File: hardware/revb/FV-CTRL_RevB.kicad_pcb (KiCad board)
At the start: 2 copper layers, 100 x 100 mm, 152 parts, among them J1 12V INPUT, J10 IR RX2 3V3/OUT/G, J11 IR TX1 A/K, J12 IR TX2 A/K, J13 LS1 DNP, J14 LS2 DNP, J15 LS3 DNP, J16 LS4 DNP, J17 I2C 3V3/SDA/SCL/G, J2 XL4015 A: 12/G/6/G, J20 SMA 50ohm ANT, J21 USB MICRO DATA, J3 XL4015 B: 12/G/6/G, J4 5V D24V25F5, J5 S1_TOP, J6 S1_BOT, J7 S2_TOP, J8 S2_BOT, J9 IR RX1 3V3/OUT/G, Q1 IRF4905PBF, Q2 P2N2222AG, Q3 MMBT3904, Q4 MMBT3904, SW1 RESET, SW2 BOOT, U1 ESP32-D0WD-V3, U2 CP2102N-A02-GQFN24, U3 LD1117V33, U4 W25Q32JVSSIQ, U5 TLV803EA30DBZR, Y1 40MHz CL10pF

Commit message: fix(hardware): replace Pololu logic supply with RECOM 5V converter
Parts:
- added C57: 10uF 50V, Capacitor_THT:CP_Radial_D5.0mm_P2.00mm, F.Cu at (120.0, 124.5)
- added C58: 100nF, Capacitor_SMD:C_0402_1005Metric, F.Cu at (118.1, 141.2)
- J4: value 5V D24V25F5 -> 5V R-78E5.0-1.0; footprint fv_reva2:Pololu_D24V25F5 -> fv_modules:RECOM_R78E5V1A
- moved J4 2.54 mm to (114.5, 138.0)
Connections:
- J4 pad 1: unconnected-(J4-Pin_1-Pad1) -> +12V
- J4 pad 2: +12V -> GND
- J4 pad 3: GND -> +5V
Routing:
- net +12V: track 128.5 -> 147.5 mm
- net +5V: track 131.4 -> 134.2 mm
- net GND: track 30.4 -> 31.1 mm, vias 41 -> 42

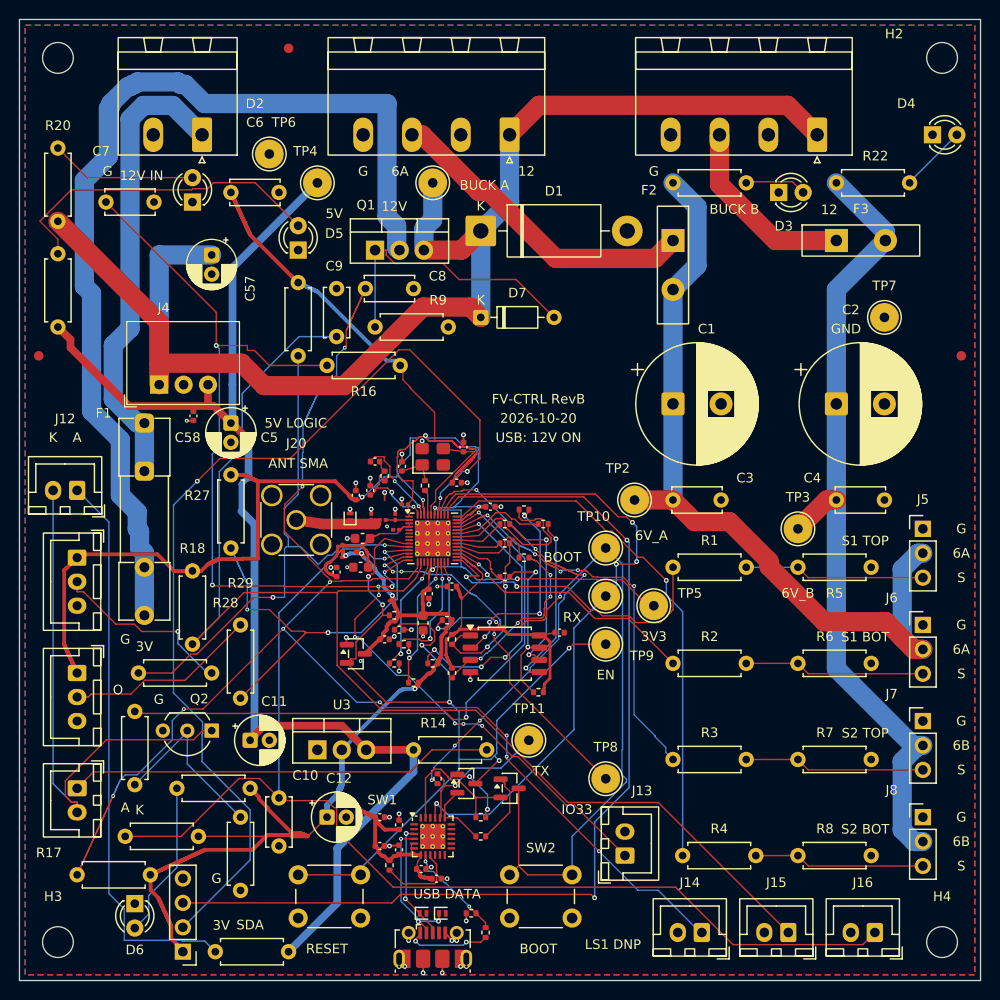
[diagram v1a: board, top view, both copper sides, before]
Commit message: feat(hardware): upgrade RevB passives to 0603 footprints and enhance DFM routing
- Convert all sub-0603 passives to 0603 footprints across schematics and PCB
- Enforce minimum track width >= 0.15mm and add safe GND stitching vias
- Verify clean schematic parity, 0 ERC errors, 0 electrical DRC errors, and via-paste clearance
- Add dedicated routing and QFN escape tools
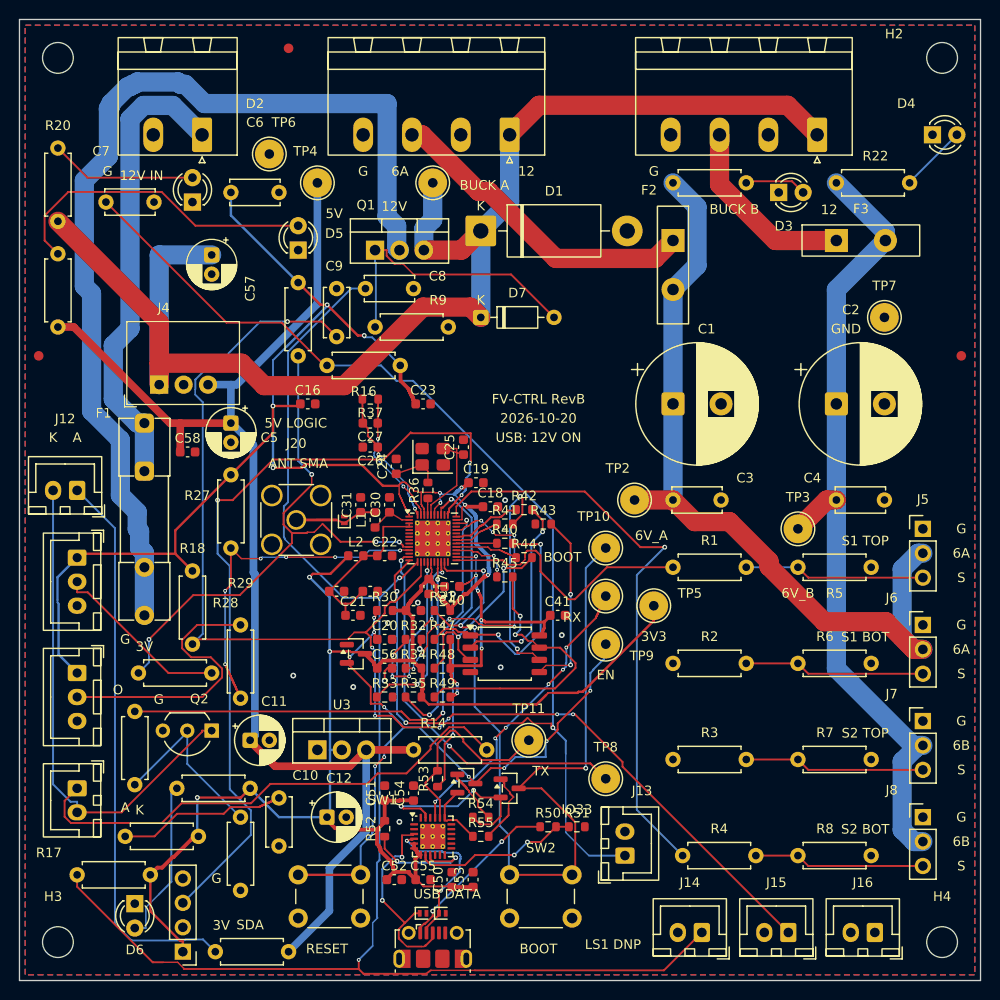
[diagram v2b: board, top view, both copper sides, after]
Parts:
- C16, C17, C18, C19, C20, C21, C24, C25, C26, C27, C40, C41, C50, C51, C52, C53, C54, C55, C56, C58: footprint Capacitor_SMD:C_0402_1005Metric -> Capacitor_SMD:C_0603_1608Metric
- C22, C23, C30, C31: footprint Capacitor_SMD:C_0201_0603Metric -> Capacitor_SMD:C_0603_1608Metric
- L1, L2: footprint Inductor_SMD:L_0201_0603Metric -> Inductor_SMD:L_0603_1608Metric
- R30, R31, R32, R33, R34, R35, R36, R37, R40, R41, R42, R43, R44, R45, R47, R48, R49, R50, R51, R52, R53, R54, R55: footprint Resistor_SMD:R_0402_1005Metric -> Resistor_SMD:R_0603_1608Metric
- moved R51 14.2 mm to (158.0, 184.0), turned to 0 degrees
- moved R50 12.8 mm to (155.0, 184.0), turned to 0 degrees
- moved C16 10.7 mm to (130.0, 140.0), turned to 0 degrees
- moved C23 10.6 mm to (142.0, 140.0), turned to 0 degrees
- moved R49 10.0 mm to (144.0, 170.5)
- moved C50 9.92 mm to (145.0, 189.5), turned to 90 degrees
- moved C53 9.58 mm to (147.2, 189.5)
- moved R37 8.14 mm to (136.5, 139.5), turned to 180 degrees
- moved C14 6.13 mm to (133.0, 159.5), turned to 0 degrees
- moved C54 6.09 mm to (141.0, 180.5)
- moved C51 5.52 mm to (138.0, 180.5), turned to 90 degrees
- moved C21 4.81 mm to (134.7, 162.0), turned to 0 degrees
- moved C26 4.50 mm to (136.5, 144.5), turned to 180 degrees
- moved C52 4.40 mm to (139.0, 189.5)
- moved C27 4.03 mm to (136.5, 142.0), turned to 180 degrees
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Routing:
- net LS4: track 125.7 -> 17.7 mm, vias 1 -> 0
- net I2C_SDA: track 103.7 -> 0.00 mm, vias 3 -> 0
- net ESP_S2_TOP_PWM: track 41.7 -> 0.00 mm, vias 5 -> 0
- net +3V3: track 351.6 -> 311.6 mm
- net UART_RX: track 67.7 -> 31.7 mm, vias 4 -> 6
- net GND: track 31.1 -> 2.92 mm, vias 42 -> 11
- net ESP_EN: track 102.0 -> 73.8 mm, vias 6 -> 10
- net ESP_S1_BOT_PWM: track 27.3 -> 0.00 mm, vias 2 -> 0
- net I2C_SCL: track 103.8 -> 85.0 mm, vias 2 -> 3
- net UART_TX_RAW: track 49.0 -> 34.5 mm, vias 6 -> 2
- net FLASH_HD: track 17.8 -> 30.5 mm
- net LS2: track 147.8 -> 159.7 mm, vias 10 -> 2
- net ESP_BOOT: track 83.1 -> 94.8 mm
- net SPI_Q: track 18.3 -> 7.40 mm
- net SPI_D: track 9.80 -> 0.00 mm
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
